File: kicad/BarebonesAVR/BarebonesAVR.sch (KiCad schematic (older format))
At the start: 14 parts, among them IC1 ATMEGA328P-P, P1 ISP6PIN, P2 CONN_FTDI_AVR, Y1 12 MHz

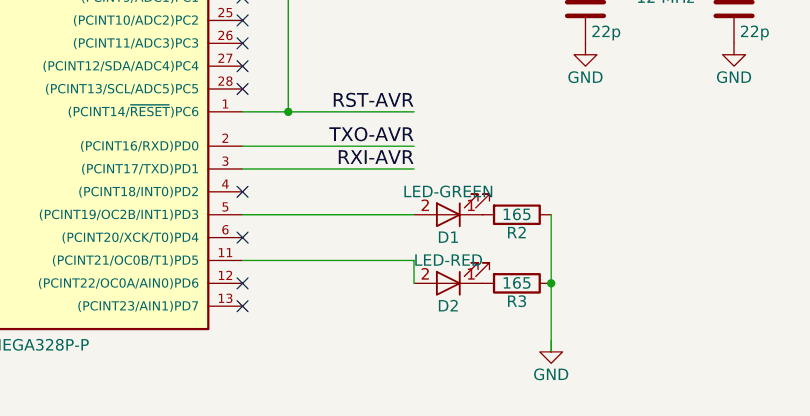
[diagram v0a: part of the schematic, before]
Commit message: Removed redundant LEDs
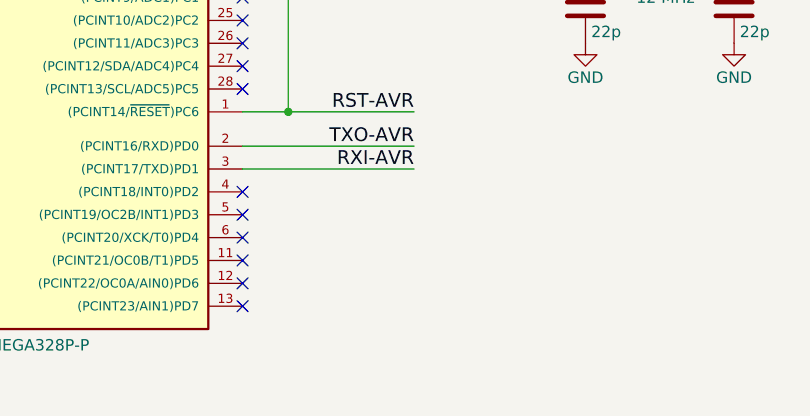
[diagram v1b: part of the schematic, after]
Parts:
- removed D1: LED-GREEN, symbol LED
- removed D2: LED-RED, symbol LED
- removed R2, R3: 165, Resistors_SMD:R_0805_HandSoldering, symbol R
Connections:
- wire segments 42 -> 38
- no-connect marks 15 -> 17
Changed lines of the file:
@@
 SPI-MOSI
-$Comp
-L R R2
-U 1 1 58ABC405
-P 5950 4350
-F 0 "R2" V 6030 4350 50  0000 C CNN
-F 1 "165" V 5950 4350 50  0000 C CNN
-F 2 "Resistors_SMD:R_0805_HandSoldering" V 5880 4350 50  0001 C CNN
-F 3 "" H 5950 4350 50  0000 C CNN
-	1    5950 4350
-	0    1    1    0
-$EndComp
-$Comp
-L R R3
-U 1 1 58ABC4EC
-P 5950 4650
-F 0 "R3" V 6030 4650 50  0000 C CNN
-F 1 "165" V 5950 4650 50  0000 C CNN
-F 2 "Resistors_SMD:R_0805_HandSoldering" V 5880 4650 50  0001 C CNN
-F 3 "" H 5950 4650 50  0000 C CNN
-	1    5950 4650
-	0    1    1    0
-$EndComp
-$Comp
-L GND #PWR8
-U 1 1 58ABC5CC
-P 6100 4900
-F 0 "#PWR8" H 6100 4650 50  0001 C CNN
-F 1 "GND" H 6100 4750 50  0000 C CNN
-F 2 "" H 6100 4900 50  0000 C CNN
-F 3 "" H 6100 4900 50  0000 C CNN
-	1    6100 4900
-	1    0    0    -1
-$EndComp
 $Comp
 L C C5
@@
 Wire Wire Line
 	4750 2750 7550 2750
-Wire Wire Line
-	4750 4550 5500 4550
-Wire Wire Line
-	5500 4550 5500 4650
-Wire Wire Line
-	4750 4350 5500 4350
-Wire Wire Line
-	6100 4350 6100 4950
-Connection ~ 6100 4650
 Connection ~ 4950 3900
 Wire Wire Line
@@
 NoConn ~ 4750 4750
 NoConn ~ 4750 3300
-$Comp
-L LED D1
-U 1 1 59F8DD2B
-P 5650 4350
-F 0 "D1" H 5650 4450 50  0000 C CNN
-F 1 "LED-GREEN" H 5650 4250 50  0000 C CNN
-F 2 "" H 5650 4350 50  0000 C CNN
-F 3 "" H 5650 4350 50  0000 C CNN
-	1    5650 4350
-	-1   0    0    1
-$EndComp
-$Comp
-L LED D2
-U 1 1 59F8DF0D
-P 5650 4650
-F 0 "D2" H 5650 4750 50  0000 C CNN
-F 1 "LED-RED" H 5650 4550 50  0000 C CNN
-F 2 "" H 5650 4650 50  0000 C CNN
-F 3 "" H 5650 4650 50  0000 C CNN
-	1    5650 4650
-	-1   0    0    1
-$EndComp
 Text Label 5500 4150 2    60   ~ 0
 RXI-AVR
@@
 NoConn ~ 4750 4250
 NoConn ~ 4750 4450
+NoConn ~ 4750 4350
+NoConn ~ 4750 4550
 $EndSCHEMATC
